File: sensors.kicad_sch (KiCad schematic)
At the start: 9 parts, among them J4 Conn_01x05_Pin, U12 CY15B064J-SXET, U3 MMC5983MA, U4 BMI088, U9 MCP23009-E/MG

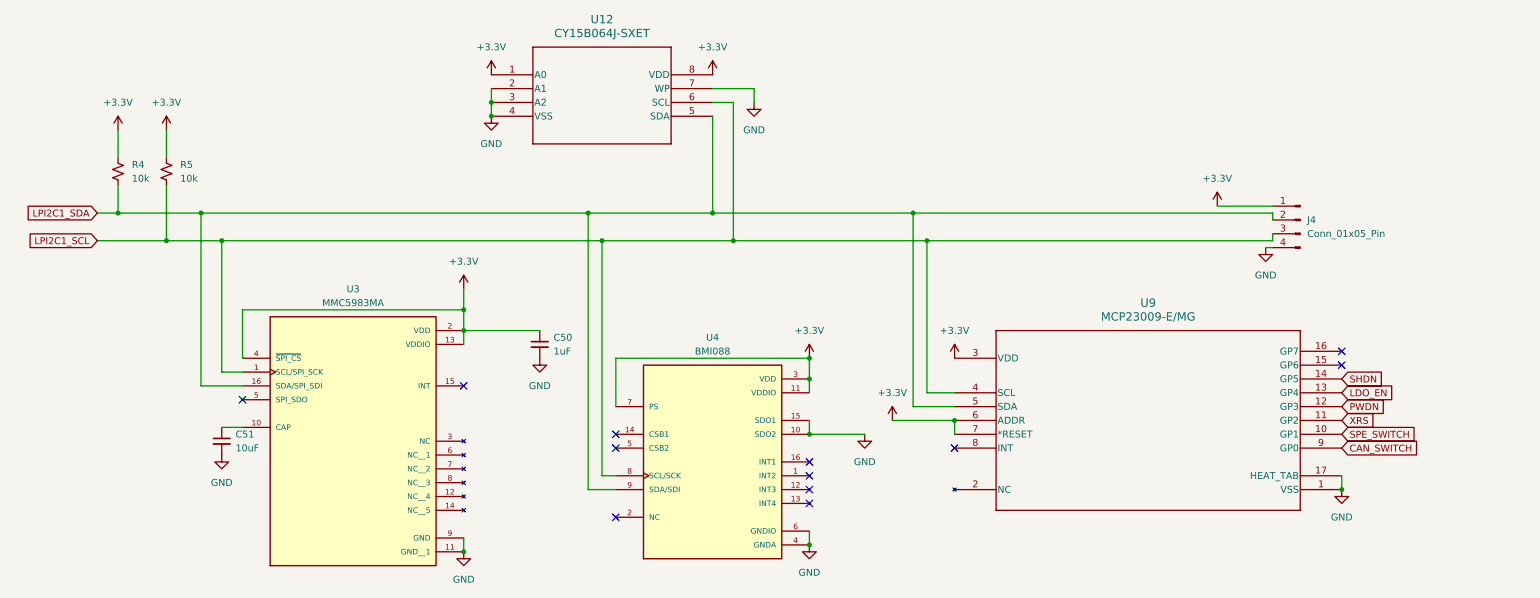
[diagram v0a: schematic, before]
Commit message: cleaned up and dealt with drc
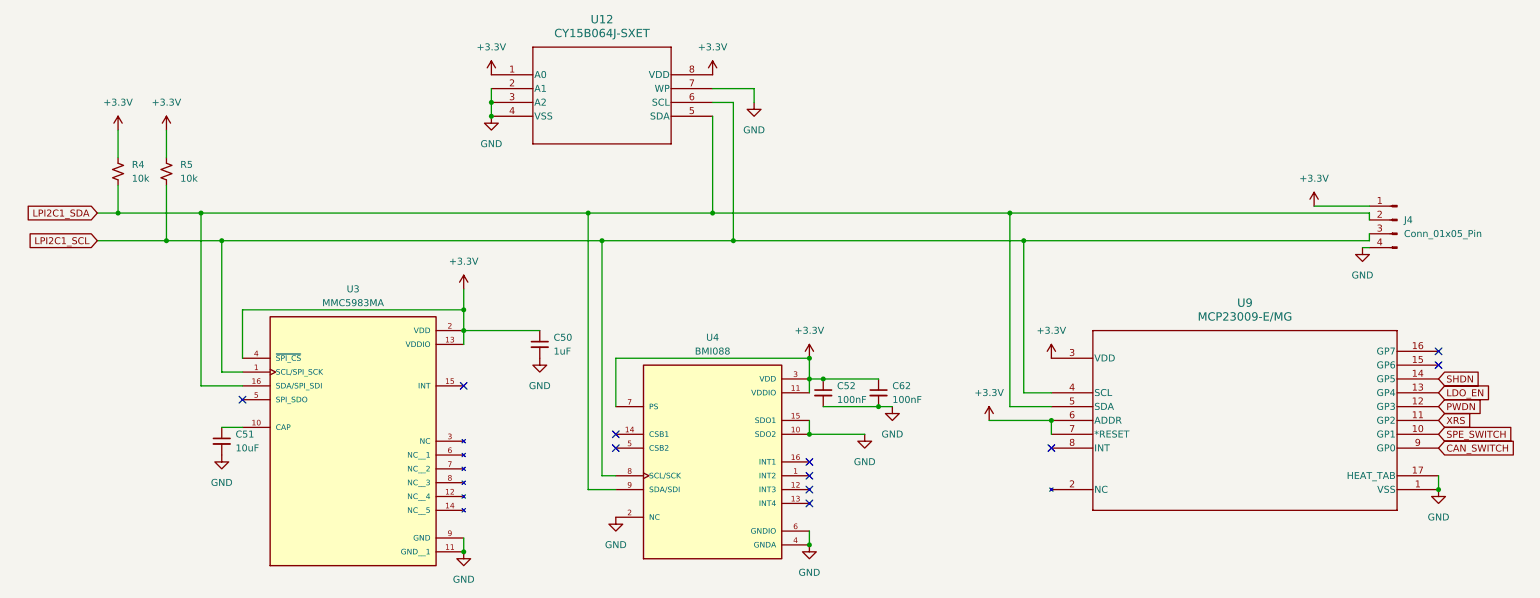
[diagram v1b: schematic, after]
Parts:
- added C52, C62: 100nF, Capacitor_SMD:C_0201_0603Metric, symbol Device:C_Small
- U3: footprint footprints:PQFN50P300X300X100-16N -> footprints:MMC5983MA_MEM
- U4: footprint footprints:PQFN50P450X300X100-16N -> footprints:QFN_BMI085_BOS
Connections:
- net +3.3V: now also C52.1, C62.1
- net GND: now also U4.2 (NC), C52.2, C62.2
- no-connect marks 12 -> 11
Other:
- moved on the sheet: J4, U9

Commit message: quick fix
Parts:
- C51: footprint Capacitor_SMD:C_0201_0603Metric -> Capacitor_SMD:C_0402_1005Metric
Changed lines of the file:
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@@
 			)
 		)
-		(property "Footprint" "Capacitor_SMD:C_0201_0603Metric"
+		(property "Footprint" "Capacitor_SMD:C_0402_1005Metric"
 			(at 55.88 140.97 0)
 			(effects
